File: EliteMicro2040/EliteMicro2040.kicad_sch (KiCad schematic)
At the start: 40 parts, among them J1 Button, J2 Button, U1 ZL6201A33S3, U2 Elite-C, U3 RP2040, Y1 3225-4P 12MHz

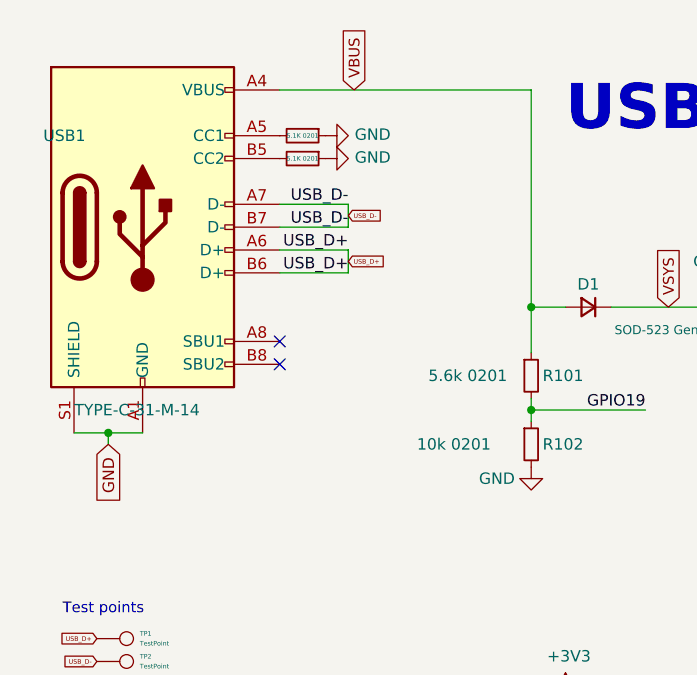
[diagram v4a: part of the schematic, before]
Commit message: Created Experimental version to fit all 0402 components and a top mount type-c port
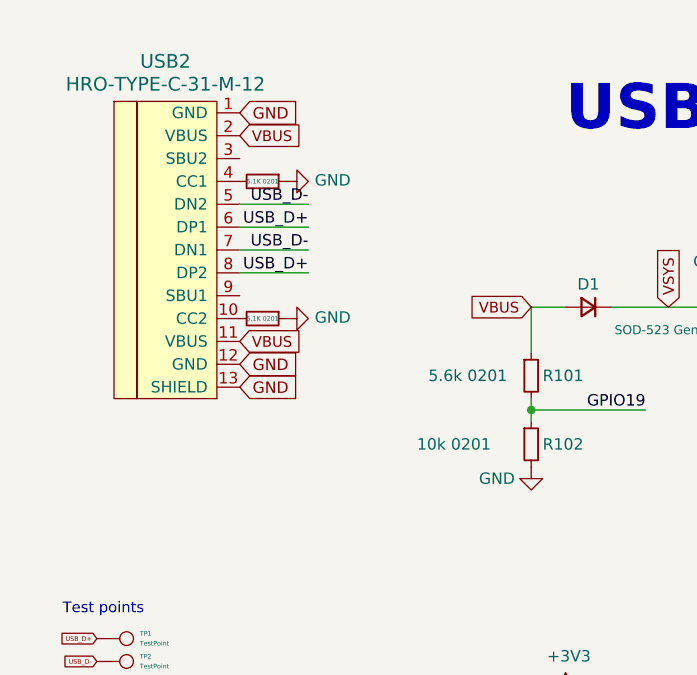
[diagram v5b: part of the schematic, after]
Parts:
- removed USB1: TYPE-C-31-M-14, josh-connectors:USB_C_TYPE-C-31-M-14, symbol josh-connector:USB_C_U262-161N-4BVC11
- added USB2: HRO-TYPE-C-31-M-12, HRO-TYPE-C31-M-12:HRO-TYPE-C-31-M-12, symbol keebio:HRO-TYPE-C-31-M-12
- C1, C10, C11, C13, C14, C15, C16, C18, C3, C4, C5, C6, C7, C8, R1, R2, R7: footprint Capacitor_SMD:C_0201_0603Metric -> Capacitor_SMD:C_0402_1005Metric
- GPIO25_LED1: footprint LED_SMD:LED_0201_0603Metric -> LED_SMD:LED_0402_1005Metric
- GPIO25_RESISTOR1, R101, R102, R3, R4, R5, R6: footprint Resistor_SMD:R_0201_0603Metric -> Resistor_SMD:R_0402_1005Metric
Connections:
- net GND: now also USB2.1 (GND), USB2.12 (GND), USB2.13 (SHIELD)
- net USB_D+: now also USB2.6 (DP1), USB2.8 (DP2)
- net USB_D-: now also USB2.5 (DN2), USB2.7 (DN1)
- net VBUS: now also USB2.11 (VBUS), USB2.2 (VBUS)
- net at R5.2: now also USB2.4 (CC1)
- net at R6.2: now also USB2.10 (CC2)
- no-connect marks 2 -> 0

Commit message: fixed up some things in the gerber, cpl and bom
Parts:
- C1, C10, C3, C4: value 1uf 0201 -> 1uf 0402
- C11, C13, C14, C15, C16, C18, C5, C6, C7, C8: value 100nf 0201 -> 100nf 0402
- GPIO25_LED1: value LED 0201 -> LED 0402
- GPIO25_RESISTOR1: value 1K 0201 -> 1K 0402
- R1, R7: value 1K 0201 -> 1K 0402; footprint Capacitor_SMD:C_0402_1005Metric -> Resistor_SMD:R_0402_1005Metric
- R101: value 5.6k 0201 -> 5.6k 0402
- R102: value 10k 0201 -> 10k 0402
- R2: value 10K 0201 -> 10K 0402; footprint Capacitor_SMD:C_0402_1005Metric -> Resistor_SMD:R_0402_1005Metric
- R3, R4: value 27r 0201 -> 27r 0402
- R5, R6: value 5.1K 0201 -> 5.1K 0402
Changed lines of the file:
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@@
       (effects (font (size 1.27 1.27)) (justify left))
     )
-    (property "Value" "10K 0201" (at 64.008 98.933 0)
-      (effects (font (size 1.27 1.27)) (justify left))
-    )
-    (property "Footprint" "Capacitor_SMD:C_0402_1005Metric" (at 60.452 97.79 90)
+    (property "Value" "10K 0402" (at 64.008 98.933 0)
+      (effects (font (size 1.27 1.27)) (justify left))
+    )
+    (property "Footprint" "Resistor_SMD:R_0402_1005Metric" (at 60.452 97.79 90)
       (effects (font (size 1.27 1.27)) hide)
     )
@@
       (effects (font (size 1.27 1.27)))
     )
-    (property "Value" "1K 0201" (at 46.99 110.0836 90)
-      (effects (font (size 1.27 1.27)))
-    )
-    (property "Footprint" "Capacitor_SMD:C_0402_1005Metric" (at 46.99 111.252 90)
+    (property "Value" "1K 0402" (at 46.99 110.0836 90)
+      (effects (font (size 1.27 1.27)))
+    )
+    (property "Footprint" "Resistor_SMD:R_0402_1005Metric" (at 46.99 111.252 90)
       (effects (font (size 1.27 1.27)) hide)
     )
@@
       (effects (font (size 1.27 1.27)) (justify left))
     )
-    (property "Value" "100nf 0201" (at 81.661 95.123 0)
+    (property "Value" "100nf 0402" (at 81.661 95.123 0)
       (effects (font (size 1.27 1.27)) (justify left))
     )
@@
       (effects (font (size 1.27 1.27)))
     )
-    (property "Value" "27r 0201" (at 245.11 93.5736 90)
+    (property "Value" "27r 0402" (at 245.11 93.5736 90)
       (effects (font (size 1.27 1.27)))
     )
@@
       (effects (font (size 1.27 1.27)))
     )
-    (property "Value" "27r 0201" (at 245.11 101.1936 90)
+    (property "Value" "27r 0402" (at 245.11 101.1936 90)
       (effects (font (size 1.27 1.27)))
     )
@@
       (effects (font (size 1.27 1.27)) (justify left))
     )
-    (property "Value" "100nf 0201" (at 237.871 67.183 0)
+    (property "Value" "100nf 0402" (at 237.871 67.183 0)
       (effects (font (size 1.27 1.27)) (justify left))
     )
@@
       (effects (font (size 1.27 1.27)) (justify left))
     )
-    (property "Value" "100nf 0201" (at 160.401 67.183 0)
+    (property "Value" "100nf 0402" (at 160.401 67.183 0)
       (effects (font (size 1.27 1.27)) (justify left))
     )
@@
       (effects (font (size 1.27 1.27)) (justify left))
     )
-    (property "Value" "100nf 0201" (at 171.831 67.183 0)
+    (property "Value" "100nf 0402" (at 171.831 67.183 0)
       (effects (font (size 1.27 1.27)) (justify left))
     )
@@
       (effects (font (size 1.27 1.27)) (justify left))
     )
-    (property "Value" "1uf 0201" (at 226.441 82.423 0)
+    (property "Value" "1uf 0402" (at 226.441 82.423 0)
       (effects (font (size 1.27 1.27)) (justify left))
     )
@@
       (effects (font (size 1.27 1.27)) (justify left))
     )
-    (property "Value" "1uf 0201" (at 95.25 35.56 90)
+    (property "Value" "1uf 0402" (at 95.25 35.56 90)
       (effects (font (size 0.508 0.508)) (justify left))
     )
@@
       (effects (font (size 1.27 1.27)) (justify left))
     )
-    (property "Value" "1uf 0201" (at 174.371 86.233 0)
+    (property "Value" "1uf 0402" (at 174.371 86.233 0)
       (effects (font (size 1.27 1.27)) (justify left))
     )
@@
       (effects (font (size 1.27 1.27)) (justify left))
     )
-    (property "Value" "100nf 0201" (at 249.301 67.183 0)
+    (property "Value" "100nf 0402" (at 249.301 67.183 0)
       (effects (font (size 1.27 1.27)) (justify left))
     )
@@
       (effects (font (size 1.27 1.27)) (justify left))
     )
-    (property "Value" "100nf 0201" (at 282.321 67.183 0)
+    (property "Value" "100nf 0402" (at 282.321 67.183 0)
       (effects (font (size 1.27 1.27)) (justify left))
     )
@@
       (effects (font (size 1.27 1.27)) (justify left))
     )
-    (property "Value" "100nf 0201" (at 270.891 67.183 0)
+    (property "Value" "100nf 0402" (at 270.891 67.183 0)
       (effects (font (size 1.27 1.27)) (justify left))
     )
@@
       (effects (font (size 1.27 1.27)) (justify left))
     )
-    (property "Value" "100nf 0201" (at 259.461 67.183 0)
+    (property "Value" "100nf 0402" (at 259.461 67.183 0)
       (effects (font (size 1.27 1.27)) (justify left))
     )
@@
       (effects (font (size 1.27 1.27)) hide)
     )
-    (property "Value" "5.1K 0201" (at 38.735 45.72 90)
+    (property "Value" "5.1K 0402" (at 38.735 45.72 90)
       (effects (font (size 0.508 0.508)))
     )
@@
       (effects (font (size 1.27 1.27)) hide)
     )
-    (property "Value" "5.1K 0201" (at 38.735 30.48 90)
+    (property "Value" "5.1K 0402" (at 38.735 30.48 90)
       (effects (font (size 0.508 0.508)))
     )
@@
       (effects (font (size 1.27 1.27)))
     )
-    (property "Value" "1K 0201" (at 365.76 192.6336 90)
+    (property "Value" "1K 0402" (at 365.76 192.6336 90)
       (effects (font (size 1.27 1.27)))
     )
@@
       (effects (font (size 1.27 1.27)))
     )
-    (property "Value" "LED 0201" (at 381 191.77 0)
+    (property "Value" "LED 0402" (at 381 191.77 0)
       (effects (font (size 1.27 1.27)))
     )
@@
       (effects (font (size 1.27 1.27)) (justify left))
     )
-    (property "Value" "1uf 0201" (at 137.16 48.26 0)
+    (property "Value" "1uf 0402" (at 137.16 48.26 0)
       (effects (font (size 0.508 0.508)) (justify left))
     )
@@
       (effects (font (size 1.27 1.27)) (justify left))
     )
-    (property "Value" "100nf 0201" (at 292.481 67.183 0)
+    (property "Value" "100nf 0402" (at 292.481 67.183 0)
       (effects (font (size 1.27 1.27)) (justify left))
     )
@@
       (effects (font (size 1.27 1.27)) (justify left))
     )
-    (property "Value" "100nf 0201" (at 301.371 67.183 0)
+    (property "Value" "100nf 0402" (at 301.371 67.183 0)
       (effects (font (size 1.27 1.27)) (justify left))
     )
@@
       (effects (font (size 1.27 1.27)) (justify left))
     )
-    (property "Value" "5.6k 0201" (at 57.15 52.07 0)
+    (property "Value" "5.6k 0402" (at 57.15 52.07 0)
       (effects (font (size 1.27 1.27)) (justify left))
     )
@@
       (effects (font (size 1.27 1.27)) (justify left))
     )
-    (property "Value" "1K 0201" (at 156.083 153.162 0)
-      (effects (font (size 1.27 1.27)) (justify left))
-    )
-    (property "Footprint" "Capacitor_SMD:C_0402_1005Metric" (at 154.94 156.718 90)
+    (property "Value" "1K 0402" (at 156.083 153.162 0)
+      (effects (font (size 1.27 1.27)) (justify left))
+    )
+    (property "Footprint" "Resistor_SMD:R_0402_1005Metric" (at 154.94 156.718 90)
       (effects (font (size 1.27 1.27)) hide)
     )
@@
       (effects (font (size 1.27 1.27)) (justify left))
     )
-    (property "Value" "10k 0201" (at 55.88 59.69 0)
-      (effects (font (size 1.27 1.27)) (justify left))
-    )
+    (property "Value" "10k 0402" (at 55.88 59.69 0)
+      (effects (font (size 1.27 1.27)) (justify left))
+    )
